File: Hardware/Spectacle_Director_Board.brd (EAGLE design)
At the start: 25.4 x 55.9 mm, 76 parts, among them J2 I2C-TRRS, J3 Serial-TRRS, Q1 310mA/60V/1.6Ω, Q2 310mA/60V/1.6Ω, U1 AP2151, U2 ATSAMD21G-A, U3 3.3V, U4 W25Q32FV, Y1 32.768kHz

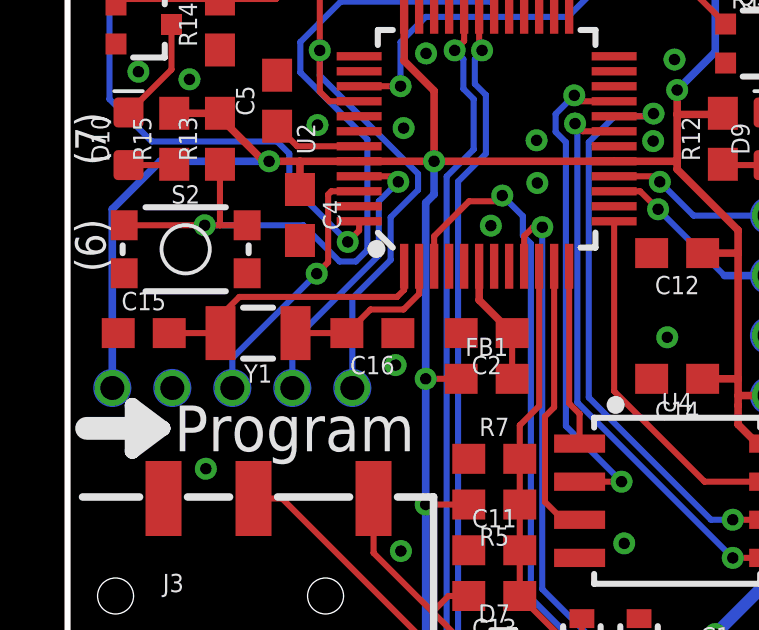
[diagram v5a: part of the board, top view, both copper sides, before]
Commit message: post-checklist fixes - minor re-routing.
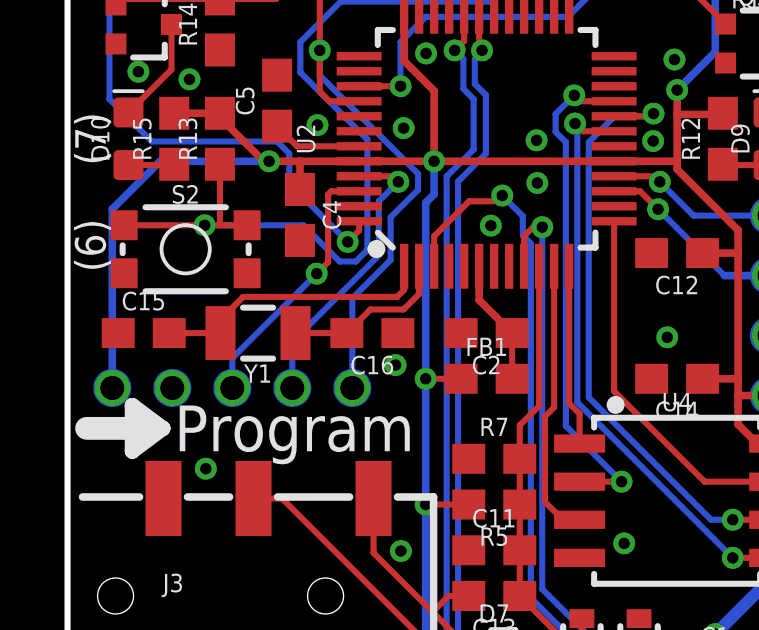
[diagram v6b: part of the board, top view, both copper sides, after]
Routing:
- net N$3: track 10.1 -> 9.58 mm
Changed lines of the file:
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@@
 <layer number="31" name="tCream" color="7" fill="4" visible="no" active="yes"/>
 <layer number="32" name="bCream" color="7" fill="5" visible="no" active="yes"/>
-<layer number="39" name="tKeepout" color="16" fill="11" visible="no" active="yes"/>
+<layer number="39" name="tKeepout" color="16" fill="11" visible="yes" active="yes"/>
 <layer number="40" name="bKeepout" color="1" fill="11" visible="no" active="yes"/>
 <layer number="41" name="tRestrict" color="4" fill="10" visible="no" active="yes"/>
@@
 <contactref element="Y1" pad="P$2"/>
 <contactref element="U2" pad="1"/>
-<wire x1="10.9855" y1="30.2895" x2="5.7277" y2="30.2895" width="0.2032" layer="1"/>
-<wire x1="5.1" y1="29.6364" x2="5.1" y2="29.083" width="0.2032" layer="1"/>
+<wire x1="10.9855" y1="30.2895" x2="5.8547" y2="30.2895" width="0.2032" layer="1"/>
+<wire x1="5.1" y1="29.6364" x2="5.1" y2="29.5348" width="0.2032" layer="1"/>
 <wire x1="3.39" y1="29.083" x2="5.1" y2="29.083" width="0.2032" layer="1"/>
-<wire x1="5.7277" y1="30.2895" x2="5.1" y2="29.6618" width="0.2032" layer="1"/>
-<wire x1="5.1" y1="29.6618" x2="5.1" y2="29.083" width="0.2032" layer="1"/>
+<wire x1="5.8547" y1="30.2895" x2="5.1" y2="29.5348" width="0.2032" layer="1"/>
+<wire x1="5.1" y1="29.5348" x2="5.1" y2="29.083" width="0.2032" layer="1"/>
 <wire x1="10.9855" y1="30.2895" x2="11.22" y2="30.524" width="0.2032" layer="1"/>
 <wire x1="11.22" y1="30.524" x2="11.22" y2="31.31" width="0.2032" layer="1"/>

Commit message: Incrementing hardware to v10. No other changes.
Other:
- board text added: "v10"
- board text removed: "v05"
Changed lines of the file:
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@@
 <layer number="31" name="tCream" color="7" fill="4" visible="no" active="yes"/>
 <layer number="32" name="bCream" color="7" fill="5" visible="no" active="yes"/>
-<layer number="39" name="tKeepout" color="16" fill="11" visible="yes" active="yes"/>
+<layer number="39" name="tKeepout" color="16" fill="11" visible="no" active="yes"/>
 <layer number="40" name="bKeepout" color="1" fill="11" visible="no" active="yes"/>
 <layer number="41" name="tRestrict" color="4" fill="10" visible="no" active="yes"/>
@@
 <dimension x1="0" y1="0" x2="0" y2="55.88" x3="-15.24" y3="27.94" textsize="1.778" textratio="15" layer="47" dtype="vertical" width="0.127" unit="inch" precision="3"/>
 <dimension x1="0" y1="0" x2="25.4" y2="0" x3="12.7" y3="-7.62" textsize="1.778" textratio="15" layer="47" dtype="horizontal" width="0.127" unit="inch" precision="3"/>
-<text x="6.985" y="0.3048" size="1.27" layer="16" font="vector" ratio="15" rot="MR0" align="bottom-center">v05</text>
+<text x="6.985" y="0.3048" size="1.27" layer="16" font="vector" ratio="15" rot="MR0" align="bottom-center">v10</text>
 <polygon width="0.2032" layer="22">
 <vertex x="19.496" y="45.031"/>
@@
 <wire x1="13.8176" y1="38.5064" x2="13.8176" y2="38.4556" width="0.2032" layer="16"/>
 <wire x1="13.8176" y1="38.4556" x2="13.5763" y2="38.2143" width="0.2032" layer="16"/>
-<wire x1="13.5763" y1="38.2143" x2="13.5763" y2="37.3888" width="0.2032" layer="16"/>
 <wire x1="13.0175" y1="34.1376" x2="13.0175" y2="14.5034" width="0.2032" layer="16"/>
-<wire x1="13.0175" y1="34.1376" x2="13.9446" y2="35.0647" width="0.2032" layer="16"/>
-<wire x1="13.9446" y1="35.0647" x2="13.9446" y2="37.0205" width="0.2032" layer="16"/>
-<wire x1="13.9446" y1="37.0205" x2="13.5763" y2="37.3888" width="0.2032" layer="16"/>
 <contactref element="J2" pad="RING1"/>
 <contactref element="D2" pad="1"/>
@@
 <wire x1="6.2" y1="12.85" x2="7.94" y2="11.11" width="0.2032" layer="1"/>
 <wire x1="7.94" y1="11.11" x2="13.732" y2="11.11" width="0.2032" layer="1"/>
+<wire x1="13.5763" y1="38.2143" x2="13.5763" y2="34.6964" width="0.2032" layer="16"/>
+<wire x1="13.5763" y1="34.6964" x2="13.0175" y2="34.1376" width="0.2032" layer="16"/>
 </signal>
 <signal name="SCL">
@@
 <wire x1="13.22" y1="38.8232" x2="12.9032" y2="38.5064" width="0.2032" layer="1"/>
 <wire x1="12.9032" y1="38.5064" x2="13.1953" y2="38.2143" width="0.2032" layer="16"/>
-<wire x1="13.1953" y1="38.2143" x2="13.1953" y2="37.2237" width="0.2032" layer="16"/>
-<wire x1="13.5382" y1="35.2044" x2="12.6365" y2="34.3027" width="0.2032" layer="16"/>
-<wire x1="13.1953" y1="37.2237" x2="13.5382" y2="36.8808" width="0.2032" layer="16"/>
-<wire x1="13.5382" y1="36.8808" x2="13.5382" y2="35.2044" width="0.2032" layer="16"/>
 <contactref element="J2" pad="RING2"/>
 <contactref element="D2" pad="2"/>
@@
 <wire x1="14.1605" y1="10.8458" x2="14.1605" y2="12.7889" width="0.2032" layer="16"/>
 <wire x1="14.1605" y1="12.7889" x2="12.6365" y2="14.3129" width="0.2032" layer="16"/>
+<wire x1="13.1953" y1="38.2143" x2="13.1953" y2="34.8615" width="0.2032" layer="16"/>
+<wire x1="13.1953" y1="34.8615" x2="12.6365" y2="34.3027" width="0.2032" layer="16"/>
 </signal>
 <signal name="RX_LED">
